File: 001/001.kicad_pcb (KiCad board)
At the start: 2 copper layers, 76.2 x 78.7 mm, 5 parts, among them SW1 SW_SPDT, U1 MF-Jalisco

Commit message: Add Battery Holder WA-BCMC and Straw Hat Led
Add Battery Holder WA-BCMC and Straw Hat Led
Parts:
- BT1: footprint 001:S8211R -> 001:WA-BCMC
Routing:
- net +3V3: track 59.2 -> 50.3 mm
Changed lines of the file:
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@@
-(kicad_pcb (version 20171130) (host pcbnew 5.1.3-ffb9f22~84~ubuntu18.04.1)
+(kicad_pcb (version 20171130) (host pcbnew 5.1.4-e60b266~84~ubuntu18.04.1)
   (general
     (thickness 1.6002)
     (drawings 0)
-    (tracks 17)
+    (tracks 15)
     (zones 0)
     (modules 5)
@@
     (descr "LED, Round, FlatTop, diameter 5.0mm, 2 pins, http://www.kingbright.com/attachments/file/psearch/000/00/00/L-483GDT(Ver.15B).pdf")
     (tags "LED Round FlatTop diameter 5.0mm 2 pins")
-    (fp_text reference D1 (at 1.27 -4.01) (layer F.SilkS)
+    (fp_text reference D1 (at 1.27 -4.01) (layer F.Fab)
       (effects (font (size 1 1) (thickness 0.15)))
     )
@@
     (pad 2 thru_hole circle (at 2.54 0) (size 1.8 1.8) (drill 0.9) (layers *.Cu *.Mask)
       (net 1 "Net-(D1-Pad2)"))
-    (model ${KISYS3DMOD}/LED_THT.3dshapes/LED_D5.0mm_FlatTop.wrl
-      (at (xyz 0 0 0))
-      (scale (xyz 1 1 1))
-      (rotate (xyz 0 0 0))
+    (model "${KISYS3DMOD}/LED_THT.3dshapes/8mm 0.5w straw hat.STEP"
+      (offset (xyz 1.3 0 2.9))
+      (scale (xyz 0.5 0.7 0.5))
+      (rotate (xyz -90 0 180))
     )
   )
@@
     (descr "LED, Round, FlatTop, diameter 5.0mm, 2 pins, http://www.kingbright.com/attachments/file/psearch/000/00/00/L-483GDT(Ver.15B).pdf")
     (tags "LED Round FlatTop diameter 5.0mm 2 pins")
-    (fp_text reference D2 (at 1.27 -4.01) (layer F.SilkS)
+    (fp_text reference D2 (at 1.27 -4.01) (layer F.Fab)
       (effects (font (size 1 1) (thickness 0.15)))
     )
@@
     (pad 1 thru_hole rect (at 0 0) (size 1.8 1.8) (drill 0.9) (layers *.Cu *.Mask)
       (net 1 "Net-(D1-Pad2)"))
-    (model ${KISYS3DMOD}/LED_THT.3dshapes/LED_D5.0mm_FlatTop.wrl
-      (at (xyz 0 0 0))
-      (scale (xyz 1 1 1))
-      (rotate (xyz 0 0 0))
-    )
-  )
-  (module 001:S8211R (layer Back)
-    (at 137.3886 105.7148)
-    (fp_text reference BT1 (at 10.16 -12.446) (layer B.SilkS)
-      (effects (font (size 1 1) (thickness 0.15)) (justify mirror))
-    )
-    (fp_text value Battery_3V_Coin (at -9.398 10.16) (layer B.Fab)
-      (effects (font (size 1 1) (thickness 0.15)) (justify mirror))
-    )
-    (fp_line (start 12.8 9.1) (end 12.8 -10.9) (layer B.SilkS) (width 0.15))
-    (fp_line (start -12.8 9.1) (end 12.8 9.1) (layer B.SilkS) (width 0.15))
-    (fp_line (start -12.8 -10.9) (end -12.8 9.1) (layer B.SilkS) (width 0.15))
-    (fp_line (start 12.8 -10.9) (end -12.8 -10.9) (layer B.SilkS) (width 0.15))
-    (pad 1 smd rect (at 12.8 0) (size 5.5 5.5) (layers Back B.Paste B.Mask)
-      (net 2 +3V3))
-    (pad 1 smd rect (at -12.8 0) (size 5.5 5.5) (layers Back B.Paste B.Mask)
-      (net 2 +3V3))
-    (pad 2 smd rect (at 0 0) (size 4 4) (layers Back B.Paste B.Mask)
-      (net 3 GND))
-    (model /home/greynaga/Desktop/kicad/packages3d/Battery.3dshapes/s8211-46r.stp
-      (offset (xyz 0 6 4))
-      (scale (xyz 1 1 1))
-      (rotate (xyz 0 90 -90))
-    )
-    (model /home/greynaga/Desktop/kicad/packages3d/Battery.3dshapes/CR-2032-01.step
-      (offset (xyz 0 0 3))
-      (scale (xyz 1 1 1))
-      (rotate (xyz 90 0 0))
+    (model "${KISYS3DMOD}/LED_THT.3dshapes/8mm 0.5w straw hat.STEP"
+      (offset (xyz 1.3 0 2.9))
+      (scale (xyz 0.5 0.7 0.5))
+      (rotate (xyz -90 0 180))
     )
   )
@@
     )
   )
-  (via (at 115.7351 102.77094) (size 0.6858) (drill 0.3302) (layers Front Back) (net 3))
+  (module 001:WA-BCMC (layer Back)
+    (at 137.3886 105.7148)
+    (fp_text reference BT1 (at 10.16 -12.446) (layer B.Fab)
+      (effects (font (size 1 1) (thickness 0.15)) (justify mirror))
+    )
+    (fp_text value Battery_3V_Coin (at -9.398 10.16) (layer B.Fab)
+      (effects (font (size 1 1) (thickness 0.15)) (justify mirror))
+    )
+    (fp_line (start 12.8 -10.9) (end -12.8 -10.9) (layer B.Fab) (width 0.15))
+    (fp_line (start -12.8 -10.9) (end -12.8 9.1) (layer B.Fab) (width 0.15))
+    (fp_line (start -12.8 9.1) (end 12.8 9.1) (layer B.Fab) (width 0.15))
+    (fp_line (start 12.8 9.1) (end 12.8 -10.9) (layer B.Fab) (width 0.15))
+    (pad 2 smd rect (at 0 0) (size 4 4) (layers Back B.Paste B.Mask)
+      (net 3 GND))
+    (pad 1 smd rect (at -12.95 0) (size 5.2 5.2) (layers Back B.Paste B.Mask)
+      (net 2 +3V3))
+    (pad 1 smd rect (at 12.95 0) (size 5.2 5.2) (layers Back B.Paste B.Mask)
+      (net 2 +3V3))
+    (model ${KISYS3DMOD}/Battery.3dshapes/s8211-46r.stp
+      (offset (xyz 0 -6 4.1))
+      (scale (xyz 1 1 1))
+      (rotate (xyz 0 90 90))
+    )
+  )
   (segment (start 130.9878 85.725) (end 143.383 85.725) (width 0.762) (layer Back) (net 1))
-  (segment (start 145.923 93.218) (end 145.923 85.725) (width 0.762) (layer Back) (net 2))
-  (segment (start 150.214 97.509) (end 145.923 93.218) (width 0.762) (layer Back) (net 2))
-  (segment (start 150.1886 97.5344) (end 150.1886 105.7148) (width 0.762) (layer Back) (net 2))
-  (segment (start 150.214 97.509) (end 150.1886 97.5344) (width 0.762) (layer Back) (net 2))
-  (segment (start 124.5886 110.1666) (end 124.5886 105.7148) (width 0.762) (layer Back) (net 2))
-  (segment (start 128.087 113.665) (end 124.5886 110.1666) (width 0.762) (layer Back) (net 2))
-  (segment (start 150.214 110.136) (end 146.685 113.665) (width 0.762) (layer Back) (net 2))
-  (segment (start 146.685 113.665) (end 128.087 113.665) (width 0.762) (layer Back) (net 2))
-  (segment (start 150.1886 110.1106) (end 150.1886 105.7148) (width 0.762) (layer Back) (net 2))
-  (segment (start 150.214 110.136) (end 150.1886 110.1106) (width 0.762) (layer Back) (net 2))
+  (segment (start 150.3386 102.0786) (end 150.3386 105.7148) (width 0.762) (layer Back) (net 2))
+  (segment (start 147.193 98.933) (end 150.3386 102.0786) (width 0.762) (layer Back) (net 2))
+  (segment (start 145.923 97.663) (end 147.193 98.933) (width 0.762) (layer Back) (net 2))
+  (segment (start 145.923 85.725) (end 145.923 97.663) (width 0.762) (layer Back) (net 2))
+  (segment (start 146.05 97.79) (end 147.193 98.933) (width 0.762) (layer Back) (net 2))
+  (segment (start 129.0014 97.79) (end 146.05 97.79) (width 0.762) (layer Back) (net 2))
+  (segment (start 124.4386 105.7148) (end 124.4386 102.3528) (width 0.762) (layer Back) (net 2))
+  (segment (start 124.4386 102.3528) (end 129.0014 97.79) (width 0.762) (layer Back) (net 2))
+  (via (at 115.7351 102.77094) (size 0.6858) (drill 0.3302) (layers Front Back) (net 3))
   (segment (start 128.4478 91.54922) (end 128.4478 85.725) (width 0.762) (layer Back) (net 4))
   (segment (start 118.74246 101.25456) (end 128.4478 91.54922) (width 0.762) (layer Back) (net 4))

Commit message: Add Gerbers
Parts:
- removed SW1: SW_SPDT, Button_Switch_SMD:SW_SPDT_PCM12
- added U2: Firma, MF-Jalisco:firma_Cu_Mask, B.Cu at (146.9, 139.1)
- added U3: PinBase, MF-Jalisco:PinBase, B.Cu at (136.7, 77.7)
- added U4: FirmaMH_Jalisco, MF-Jalisco:001_firma_MF, F.Cu at (159.7, 82.6)
- D1, D2: footprint LED_THT:LED_D5.0mm_FlatTop -> MF-Jalisco:LED_D5.0mm_FlatTop
- U1: footprint 001:MF-Jalisco-001 -> MF-Jalisco:MF-Jalisco-001
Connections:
- D1 pad 1: Net-(D1-Pad1) -> GND
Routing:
- net Net-(D1-Pad1): track 26.2 -> 0.00 mm
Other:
- board text added: "+"
- board text added: "Developed by"

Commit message: update
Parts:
- removed U4: FirmaMH_Jalisco, MF-Jalisco:001_firma_MF
- BT1: footprint 001:WA-BCMC -> MF-Jalisco:WA-BCMC
- U1: footprint MF-Jalisco:MF-Jalisco-001 -> MF-Jalisco:MF-Jalisco_50mm
- moved U2 16.0 mm to (143.9, 123.4)
- moved D1 5.36 mm to (131.4, 90.2)
- moved D2 5.06 mm to (141.0, 90.2)
- moved U3 4.19 mm to (137.2, 81.9)
- moved BT1 4.09 mm to (137.5, 101.6)
- moved U1 3.25 mm to (137.2, 100.3)
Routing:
- net +3V3: track 50.3 -> 0.00 mm
- net Net-(D1-Pad2): track 12.4 -> 0.00 mm
- net GND: vias 1 -> 0
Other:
- board size 76.2 x 78.7 mm -> 47.6 x 49.1 mm
- board text removed: "+"
- board text removed: "Developed by"

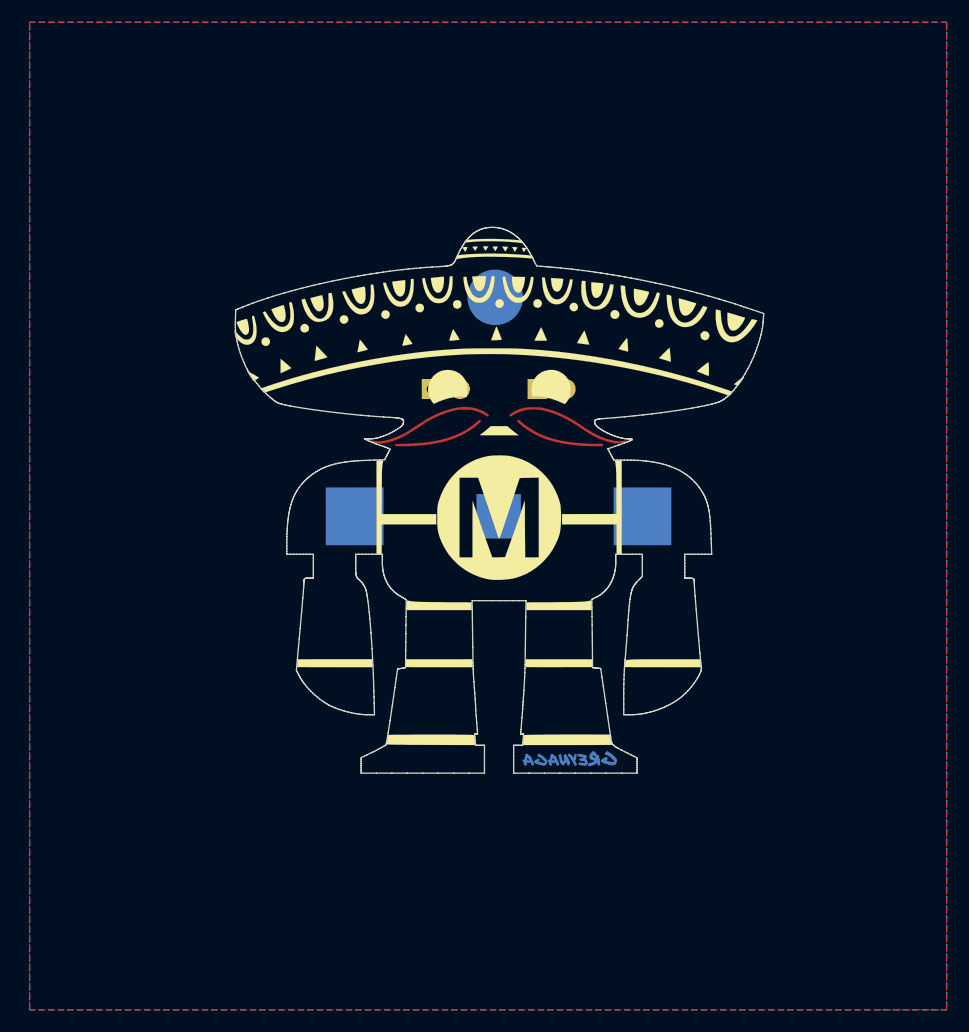
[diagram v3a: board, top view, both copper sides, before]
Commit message: Update battery holder
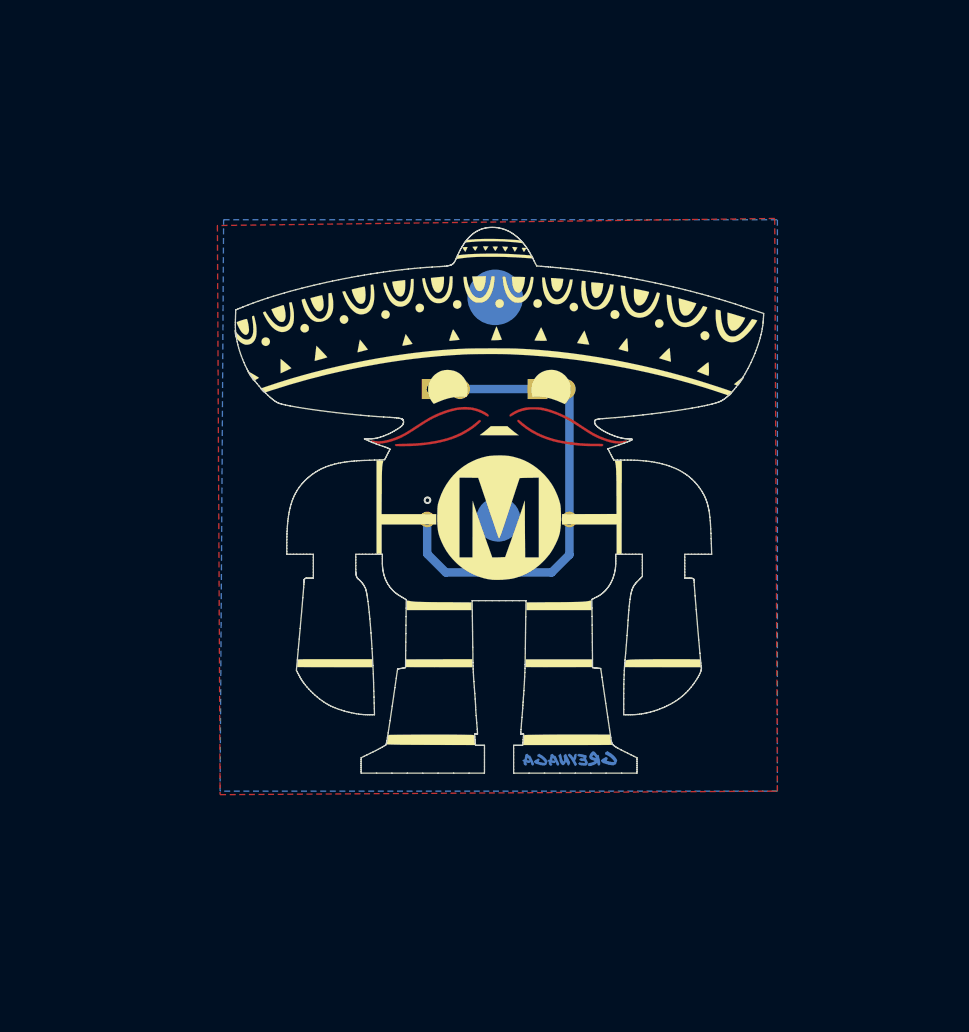
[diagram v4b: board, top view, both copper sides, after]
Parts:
- added Ref**: Val**, MF-Jalisco:MF-Jalisco_Logo_50mmsvg, F.Cu at (123.1, 87.9)
- BT1: footprint MF-Jalisco:WA-BCMC -> MF-Jalisco:CR1220-Jalisco
- moved BT1 0.28 mm to (137.4, 101.9)
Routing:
- net +3V3: track 0.00 -> 32.3 mm
- net Net-(D1-Pad2): track 0.00 -> 6.98 mm
- net GND: vias 0 -> 1
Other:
- board text added: "Developed by"

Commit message: Add patrocinador X logo
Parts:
- added Ref**: Val**, MF-Jalisco:MF-Jalisco_Logo_PatrocinioX_50mmsvg, F.Cu at (153.7, 87.0)

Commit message: Changes
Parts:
- removed the Ref** at (153.7, 87.0)
- removed the Ref** at (123.1, 87.9)
- removed U1: MF-Jalisco, MF-Jalisco:MF-Jalisco_50mm
- added Ref**: Val**, MF-ROME:Rome_100mm_01, F.Cu at (134.0, 102.9)
- BT1: footprint MF-Jalisco:CR1220-Jalisco -> MF-ROME:S8211R
- D1, D2: footprint MF-Jalisco:LED_D5.0mm_FlatTop -> MF-ROME:LED_D5.0mm_FlatTop
- U2: footprint MF-Jalisco:firma_Cu_Mask -> MF-ROME:firma_Cu_Mask
- U3: footprint MF-Jalisco:PinBase -> MF-ROME:PinBase
- moved U2 29.9 mm to (118.7, 139.7)
- moved D1 16.8 mm to (121.8, 76.5)
- moved D2 13.7 mm to (140.6, 76.5)
- moved U3 13.1 mm to (132.1, 69.8)
- moved BT1 3.58 mm to (134.6, 99.7), turned to 180 degrees
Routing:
- net +3V3: track 32.3 -> 0.00 mm
- net Net-(D1-Pad2): track 6.98 -> 0.00 mm
- net GND: vias 1 -> 0
- removed copper zone on B.Cu, net GND
- removed copper zone on F.Cu, net GND
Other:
- board size 47.6 x 49.1 mm -> 76 x 84.5 mm
- board text removed: "Developed by"
